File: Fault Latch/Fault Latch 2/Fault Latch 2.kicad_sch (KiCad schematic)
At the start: 63 parts, among them J101 Inputs, K103 Fujitsu_FTR-LYAA005x, K104 Fujitsu_FTR-LYAA005x, K105 Fujitsu_FTR-LYAA005x, Q1 PMOS, Q101 NMOS, Q104 NMOS, Q108 NMOS, Q109 NMOS, Q110 NMOS, Q2 PMOS, Q3 NPN, Q4 NPN, Q5 NPN, Q6 NPN, Q7 NPN, Q8 NPN, SW4 SW_Omron_B3FS, SW5 SW_Omron_B3FS, SW6 SW_Omron_B3FS, U103 74AHC1G00, U104 74LS279, U105 SFH617A-1, U106 74AHC1G00, U108 SFH617A-1, U109 74AHC1G00, U111 SFH617A-1

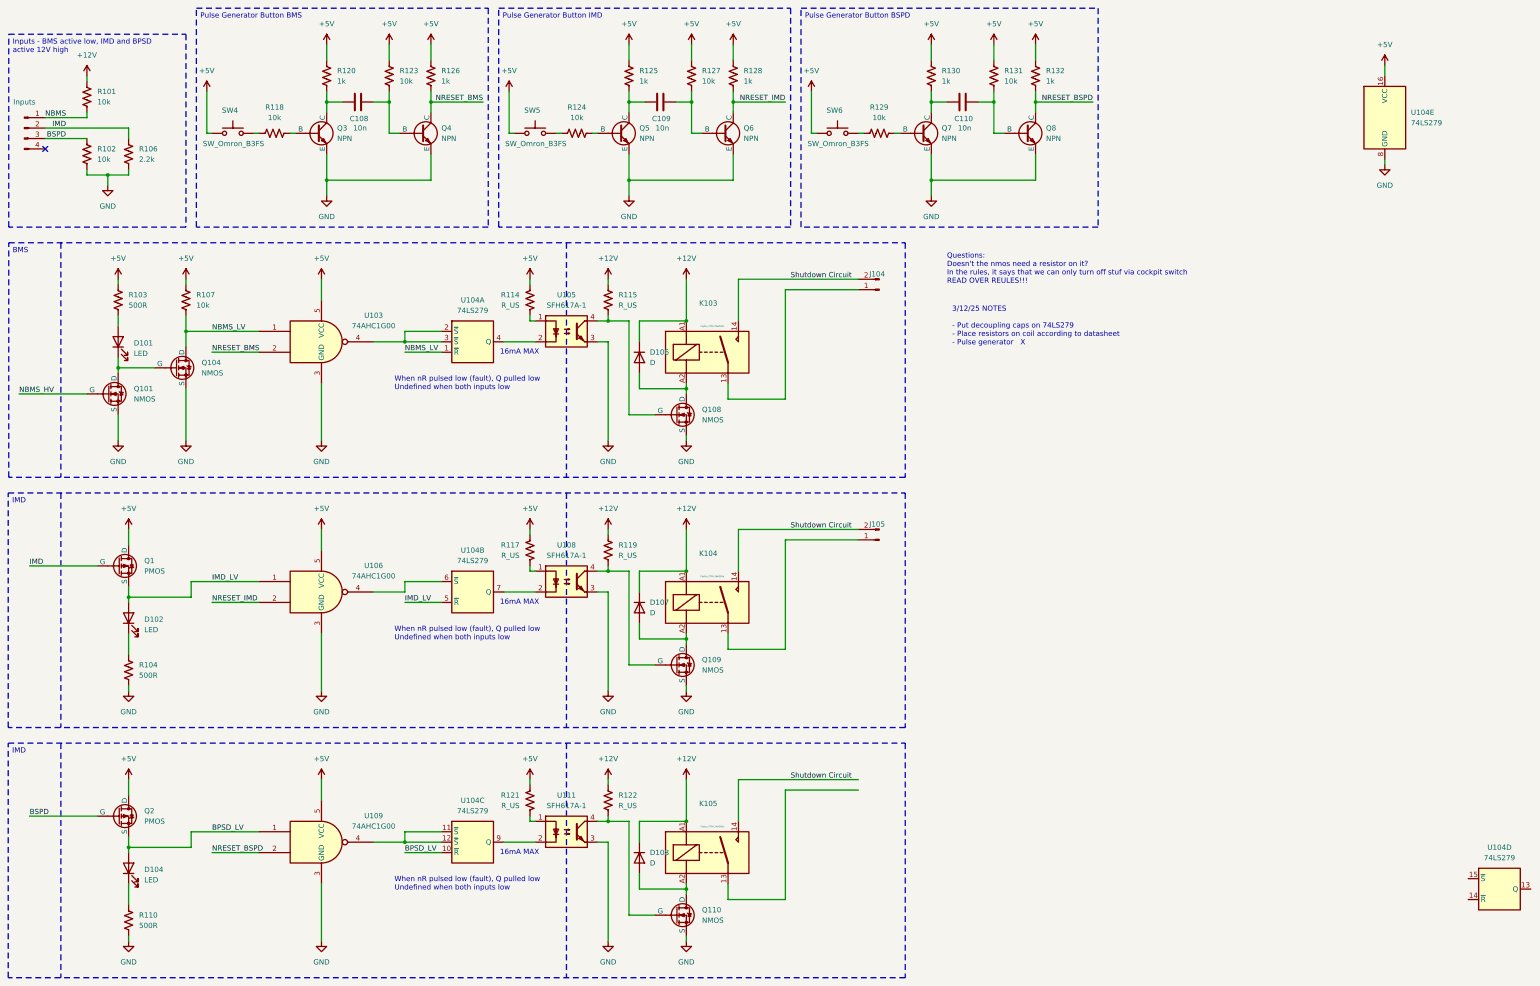
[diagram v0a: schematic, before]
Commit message: Added decoup capacitor
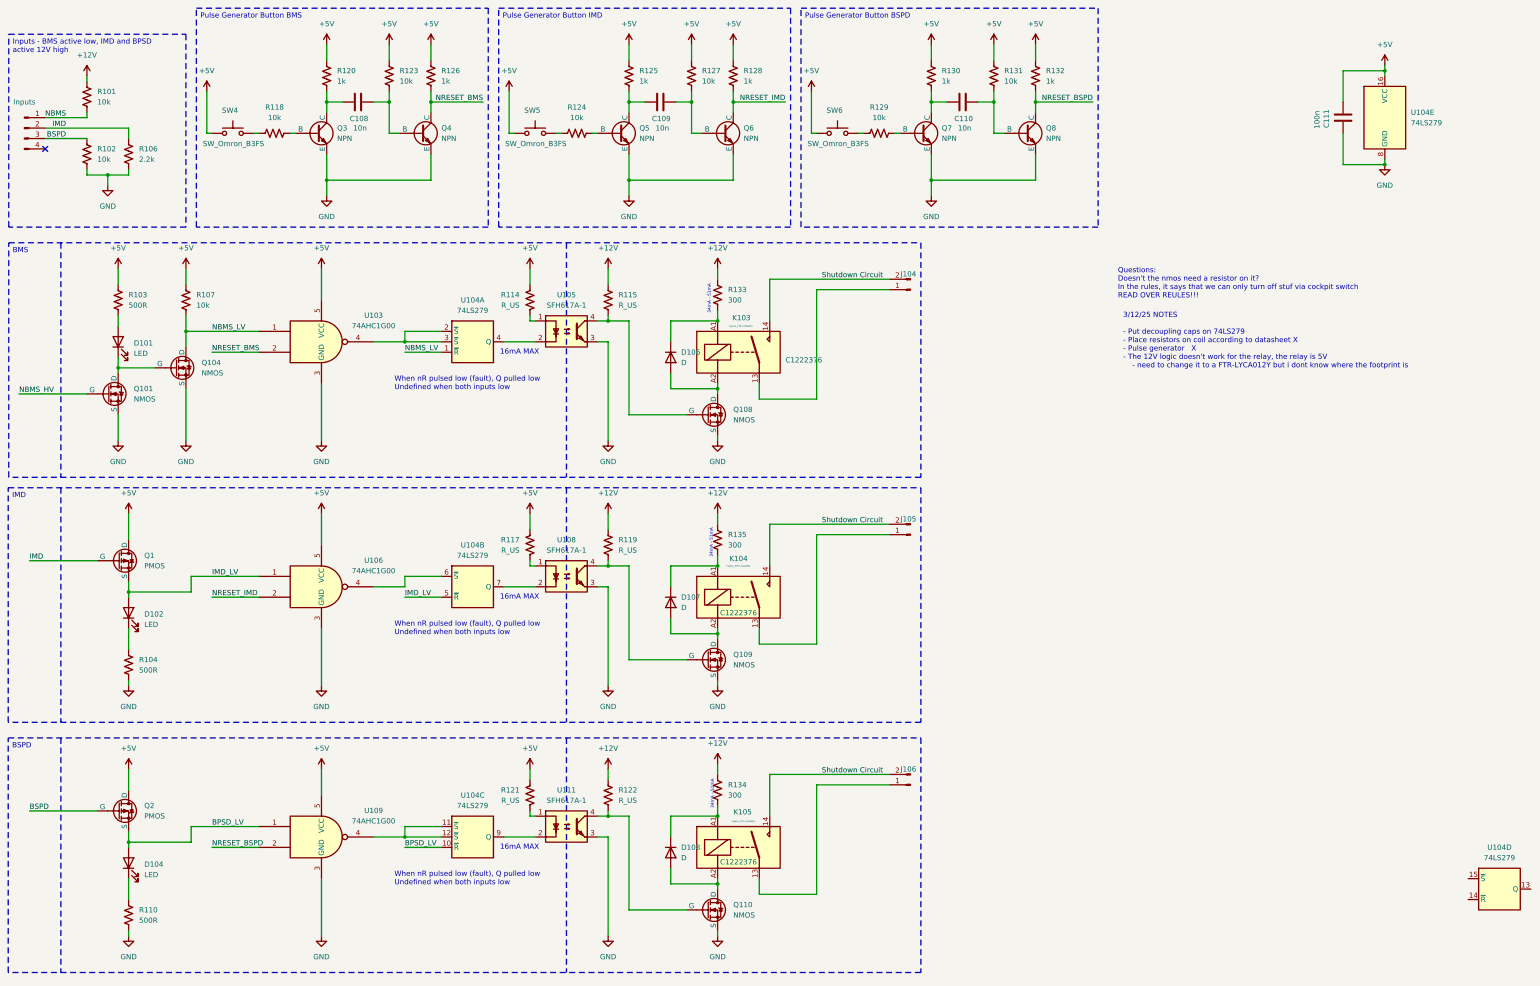
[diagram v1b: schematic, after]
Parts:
- added C111: 100n, symbol Device:C
- added J106: ~, symbol Connector:Conn_01x02_Pin
- added R133, R134, R135: 300, symbol Device:R_US
- K103, K104, K105: JLC# (none) -> C1222376
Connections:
- net +12V: now also R133.1, R134.1, R135.1; no longer D106.1 (K), D107.1 (K), D108.1 (K), K103.A1, K104.A1, K105.A1
- net +5V: now also C111.1
- net GND: now also C111.2
- net Shutdown Circuit: now also J106.2 (Pin_2)
- net at K105.13: now also J106.1 (Pin_1)
- new net: D106.1 (K), K103.A1, R133.2
- new net: D108.1 (K), K105.A1, R134.2
- new net: D107.1 (K), K104.A1, R135.2
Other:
- note added: "3/12/25 NOTES - Put decoupling caps on 74LS279 - Place resistors on coil according to datasheet X - Pulse generator X - The 12V logic doesn't work for the relay, the relay is 5V - need to change it to a FTR-LYCA012Y but i dont know where the footprint is"
- note added: "34mA - 51mA"
- note removed: "3/12/25 NOTES - Put decoupling caps on 74LS279 - Place resistors on coil according to datasheet - Pulse generator X"
- moved on the sheet: D102, D104, D106, D107, D108, J104, J105, K103, K104, K105, Q1, Q108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

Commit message: Fault Latch Overhaul
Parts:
- removed D101, D104: LED, LED_SMD:LED_0201_0603Metric, symbol Device:LED
- removed D106, D107, D108: D, symbol Device:D
- removed J101: Inputs, symbol Connector:Conn_01x04_Pin
- removed J104, J105, J106: ~, symbol Connector:Conn_01x02_Pin
- removed Q1, Q2: PMOS, symbol Simulation_SPICE:PMOS
- removed Q101, Q104, Q108, Q109, Q110: NMOS, symbol Simulation_SPICE:NMOS
- removed Q3, Q4, Q5, Q6, Q7, Q8: NPN, symbol Simulation_SPICE:NPN
- removed R102: 10k, symbol Device:R_US
- removed R103, R110: 500R, symbol Device:R_US
- removed R106: 2.2k, symbol Device:R_US
- removed R133, R134: 300, symbol Device:R_US
- removed SW4, SW5: SW_Omron_B3FS, Button_Switch_SMD:SW_SPST_Omron_B3FS-100xP, symbol Switch:SW_Omron_B3FS
- added C102, C103, C104, C110: 100n, Capacitor_SMD:C_0603_1608Metric_Pad1.08x0.95mm_HandSolder, symbol Device:C
- added C107: 47u, Capacitor_SMD:CP_Elec_6.3x5.4, symbol Device:C
- added C108: 1u, Capacitor_SMD:C_0805_2012Metric_Pad1.18x1.45mm_HandSolder, symbol Device:C
- added C109: 0.33u, Capacitor_SMD:C_0603_1608Metric_Pad1.08x0.95mm_HandSolder, symbol Device:C
- added D102, D103: RED, LED_SMD:LED_0805_2012Metric_Pad1.15x1.40mm_HandSolder, symbol Device:LED
- added D104, D105, D106: D_Schottky, Diode_SMD:D_SMA, symbol Device:D_Schottky
- added H101, H102, H103, H104: MountingHole, MountingHole:MountingHole_3.2mm_M3, symbol Mechanical:MountingHole
- added PS101: RI-1205S, DC-DC:RI0505S, symbol DC-DC:RI-1205S
- added Q104, Q106, Q107, Q108, Q112, Q113: Q_NPN_BEC, Package_TO_SOT_SMD:SOT-23, symbol Transistor_BJT:Q_NPN_BEC
- added Q109, Q110, Q111: Q_NMOS_GDS, Package_TO_SOT_SMD:TO-252-2, symbol Transistor_FET:Q_NMOS_GDS
- added R105: 270R, Resistor_SMD:R_0805_2012Metric_Pad1.20x1.40mm_HandSolder, symbol Device:R_US
- added R112, R124: 100k, Resistor_SMD:R_0805_2012Metric_Pad1.20x1.40mm_HandSolder, symbol Device:R_US
- added R129: 10k, Resistor_SMD:R_0805_2012Metric_Pad1.20x1.40mm_HandSolder, symbol Device:R_US
- added R131: 2.2k, Resistor_SMD:R_0805_2012Metric_Pad1.20x1.40mm_HandSolder, symbol Device:R_US
- added SW101, SW102: SW_Omron_B3FS, Button_Switch_SMD:SW_SPST_Omron_B3FS-100xP, symbol Switch:SW_Omron_B3FS
- added U101, U105, U110, U111, U112, U113: 641964-1, 641964-1:TE_641964-1, symbol CONNECTOR:641964-1
- added U114, U115, U116: SFH617A-1, Package_DIP:DIP-4_W7.62mm, symbol Isolator:SFH617A-1
- C101: renamed from C108; footprint (none) -> Capacitor_SMD:C_0603_1608Metric_Pad1.08x0.95mm_HandSolder; JLC# (none) -> C1589
- C105: renamed from C109; footprint (none) -> Capacitor_SMD:C_0603_1608Metric_Pad1.08x0.95mm_HandSolder; JLC# (none) -> C1589
- C106: renamed from C110; footprint (none) -> Capacitor_SMD:C_0603_1608Metric_Pad1.08x0.95mm_HandSolder; JLC# (none) -> C1589
- C111: footprint (none) -> Capacitor_SMD:C_0603_1608Metric_Pad1.08x0.95mm_HandSolder; JLC# (none) -> C1591
- D101: renamed from D102; value LED -> RED; footprint LED_SMD:LED_0201_0603Metric -> LED_SMD:LED_0805_2012Metric_Pad1.15x1.40mm_HandSolder; JLC# IN-S21AT2G -> C19171391
- R101: value 10k -> 100k; footprint (none) -> Resistor_SMD:R_0805_2012Metric_Pad1.20x1.40mm_HandSolder; JLC# (none) -> C149504
- R102: renamed from R118; footprint (none) -> Resistor_SMD:R_0805_2012Metric_Pad1.20x1.40mm_HandSolder; JLC# (none) -> C17414
- R104: value 500R -> 270R; footprint (none) -> Resistor_SMD:R_0805_2012Metric_Pad1.20x1.40mm_HandSolder; JLC# (none) -> C17590
- R106: renamed from R120; footprint (none) -> Resistor_SMD:R_0805_2012Metric_Pad1.20x1.40mm_HandSolder; JLC# (none) -> C17513
- R107: value 10k -> 270R; footprint (none) -> Resistor_SMD:R_0805_2012Metric_Pad1.20x1.40mm_HandSolder; JLC# (none) -> C17590
- R108: renamed from R123; value 10k -> 100k; footprint (none) -> Resistor_SMD:R_0805_2012Metric_Pad1.20x1.40mm_HandSolder; JLC# (none) -> C149504
- R109: renamed from R126; footprint (none) -> Resistor_SMD:R_0805_2012Metric_Pad1.20x1.40mm_HandSolder; JLC# (none) -> C17513
- R113: renamed from R124; footprint (none) -> Resistor_SMD:R_0805_2012Metric_Pad1.20x1.40mm_HandSolder; JLC# (none) -> C17414
- R114: renamed from R125; footprint (none) -> Resistor_SMD:R_0805_2012Metric_Pad1.20x1.40mm_HandSolder; JLC# (none) -> C17513
- R115: renamed from R127; value 10k -> 100k; footprint (none) -> Resistor_SMD:R_0805_2012Metric_Pad1.20x1.40mm_HandSolder; JLC# (none) -> C149504
- R116: renamed from R114; value R_US -> 270R; footprint (none) -> Resistor_SMD:R_0805_2012Metric_Pad1.20x1.40mm_HandSolder; JLC# (none) -> C17590
- R117: value R_US -> 270R; footprint (none) -> Resistor_SMD:R_0805_2012Metric_Pad1.20x1.40mm_HandSolder; JLC# (none) -> C17590
- R118: renamed from R121; value R_US -> 270R; footprint (none) -> Resistor_SMD:R_0805_2012Metric_Pad1.20x1.40mm_HandSolder; JLC# (none) -> C17590
- R120: renamed from R128; footprint (none) -> Resistor_SMD:R_0805_2012Metric_Pad1.20x1.40mm_HandSolder; JLC# (none) -> C17513
- R121: renamed from R115; value R_US -> 10k; footprint (none) -> Resistor_SMD:R_0805_2012Metric_Pad1.20x1.40mm_HandSolder; JLC# (none) -> C17414
- R122: renamed from R119; value R_US -> 10k; footprint (none) -> Resistor_SMD:R_0805_2012Metric_Pad1.20x1.40mm_HandSolder; JLC# (none) -> C17414
- R123: renamed from R122; value R_US -> 10k; footprint (none) -> Resistor_SMD:R_0805_2012Metric_Pad1.20x1.40mm_HandSolder; JLC# (none) -> C17414
- R125: renamed from R129; footprint (none) -> Resistor_SMD:R_0805_2012Metric_Pad1.20x1.40mm_HandSolder; JLC# (none) -> C17414
- R126: renamed from R130; footprint (none) -> Resistor_SMD:R_0805_2012Metric_Pad1.20x1.40mm_HandSolder; JLC# (none) -> C17513
- R127: renamed from R131; value 10k -> 100k; footprint (none) -> Resistor_SMD:R_0805_2012Metric_Pad1.20x1.40mm_HandSolder; JLC# (none) -> C149504
- R128: renamed from R132; footprint (none) -> Resistor_SMD:R_0805_2012Metric_Pad1.20x1.40mm_HandSolder; JLC# (none) -> C17513
- R135: value 300 -> 10k; footprint (none) -> Resistor_SMD:R_0805_2012Metric_Pad1.20x1.40mm_HandSolder; JLC# (none) -> C17414
- U102: renamed from U103; footprint (none) -> Package_TO_SOT_SMD:SOT-23-5; JLC# (none) -> C350556
- U103: renamed from U106; footprint (none) -> Package_TO_SOT_SMD:SOT-23-5; JLC# (none) -> C350556
- U104: renamed from U109; footprint (none) -> Package_TO_SOT_SMD:SOT-23-5; JLC# (none) -> C350556
- U106: renamed from U104; MOUSER (none) -> 595-SN74LS279ADR
- U107: renamed from U105; MOUSER (none) -> SFH617A-1X007T
- U108: MOUSER (none) -> SFH617A-1X007T
- U109: renamed from U111; MOUSER (none) -> SFH617A-1X007T
- renumbered K103 to K101, K104 to K102, K105 to K103, SW6 to SW103
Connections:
- net NBMS is gone; now on net GND: R101.2
- net +12V: now also K101.A1, K102.A1, K103.A1, C107.2, C108.2, C109.2, D104.1 (K), D105.1 (K), D106.1 (K), PS101.1 (-VIN), R129.2, U113.1; no longer R101.1, R135.1
- net +5V: now also R104.1, SW103.2, C102.1, C103.1, C104.1, C110.2, PS101.4 (+VOUT), R105.1, SW101.2, SW102.2; no longer SW103.1
- net GND: now also C102.2, C103.2, C104.2, C110.1, PS101.3 (-VOUT), Q104.2 (E), Q106.2 (E), Q107.2 (E), Q108.2 (E), Q112.2 (E), Q113.2 (E), R112.2, R124.2, U114.3, U115.3, U116.3; no longer R104.2, U107.3, U108.3, U109.3
- net NBMS_HV: now also U101.2, U114.2
- net NBMS_LV: now also D103.1 (K), U114.4; no longer R107.2
- net NRESET_BMS: now also Q106.3 (C)
- net NRESET_BSPD: now also Q113.3 (C)
- net NRESET_IMD: now also Q108.3 (C)
- net at K103.13: now also U112.1
- net at C105.1, R114.2: now also Q107.3 (C)
- net at R113.1: now also Q107.1 (B)
- net at K101.13: now also U110.1
- net at K101.A2: now also D104.2 (A), Q109.2 (D)
- net at C101.1, R106.2: now also Q104.3 (C)
- net at R102.1: now also Q104.1 (B)
- net at K103.A2: now also D106.2 (A), Q111.2 (D)
- net at C106.1, R126.2: now also Q112.3 (C)
- net at R125.1: now also Q112.1 (B)
- net at R113.2: now also R112.1, SW102.1
- net at C106.2, R127.2: now also Q113.1 (B)
- net at C105.2, R115.2: now also Q108.1 (B)
- net at R135.2: now also U116.2; no longer K102.A1
- net at K102.A2: now also D105.2 (A), Q110.2 (D)
- net NIMD_LV: now reaches D101.1 (K)
- net NIMD_LV: now also U103.1, U106.5 (~{R}), U115.4; no longer R104.1
- net at R121.1, U107.4: now also Q109.1 (G)
- net at R122.1, U108.4: now also Q110.1 (G)
- net at C101.2, R108.2: now also Q106.1 (B)
- net at R123.1, U109.4: now also Q111.1 (G)
- net at R102.2: now also R101.1, SW101.1
- net at K102.13: now also U111.1
- net at R125.2: now also SW103.1, R124.1; no longer SW103.2
- net BPSD_LV renamed NBPSD_LV
- net NBPSD_LV: now also D102.1 (K), U116.4
- removed net IMD_LV: D101.2 (A), U103.1, U106.5 (~{R})
- removed net Shutdown Circuit: K101.14, K102.14, K103.14
- new net: K101.14, U110.2
- new net: R129.1, U114.1
- new net: D102.2 (A), R105.2
- new net: K102.14, U111.2
- new net: K103.14, U112.2
- new net: R131.1, U115.2
- new net: D101.2 (A), R104.2
- new net: D103.2 (A), R107.2
- new net BSPD_HV: U105.2, U116.1
- new net GNDPWR: C107.1, C108.1, C109.1, PS101.2 (+VIN), Q109.3 (S), Q110.3 (S), Q111.3 (S), R131.2, R135.1, U107.3, U108.3, U109.3, U113.2
- new net IMD_HV: U105.1, U115.1
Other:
- note added: "12V"
- note removed: "34mA - 51mA"
- moved on the sheet: C101, C105, C106, C111, D101, K101, K102, K103, R102, R104, R106, R107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

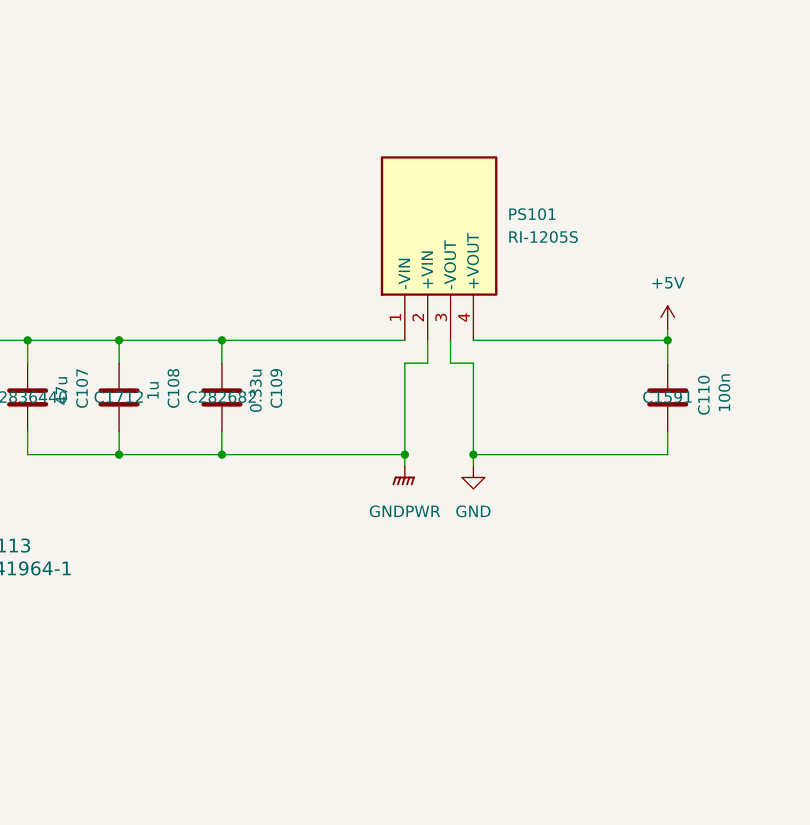
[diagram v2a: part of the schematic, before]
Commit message: Found jlcpart for dcdc converter. It's chinese
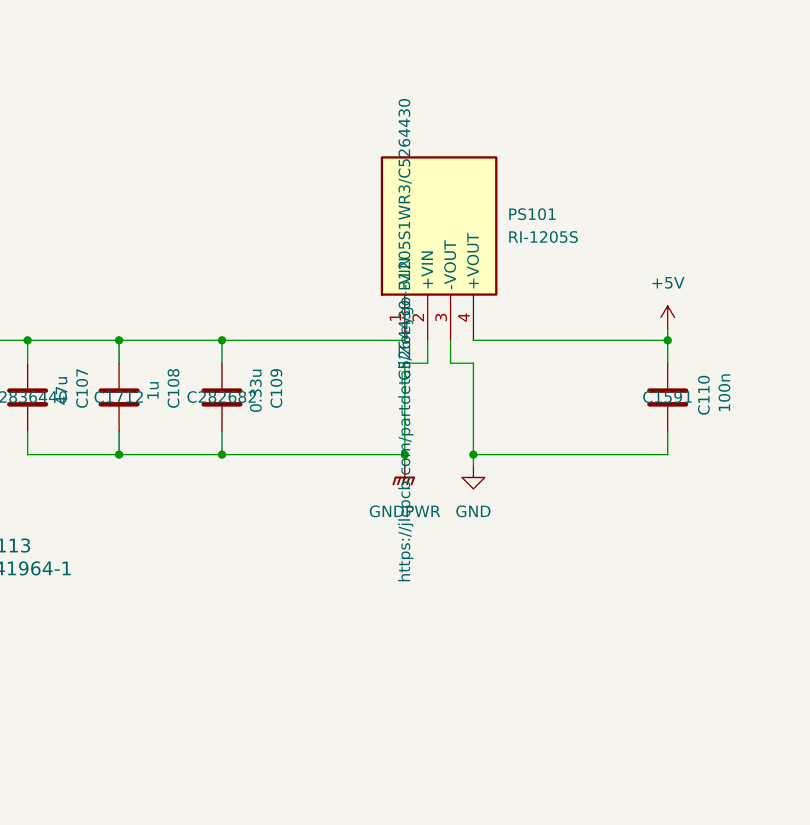
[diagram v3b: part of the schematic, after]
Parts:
- PS101: JLC# (none) -> C5264430; Notes (none) -> https://jlcpcb.com/partdetail/Zoeygo-B1205S1WR3/C5264430
